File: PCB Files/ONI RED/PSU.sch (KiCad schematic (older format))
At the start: 10 parts

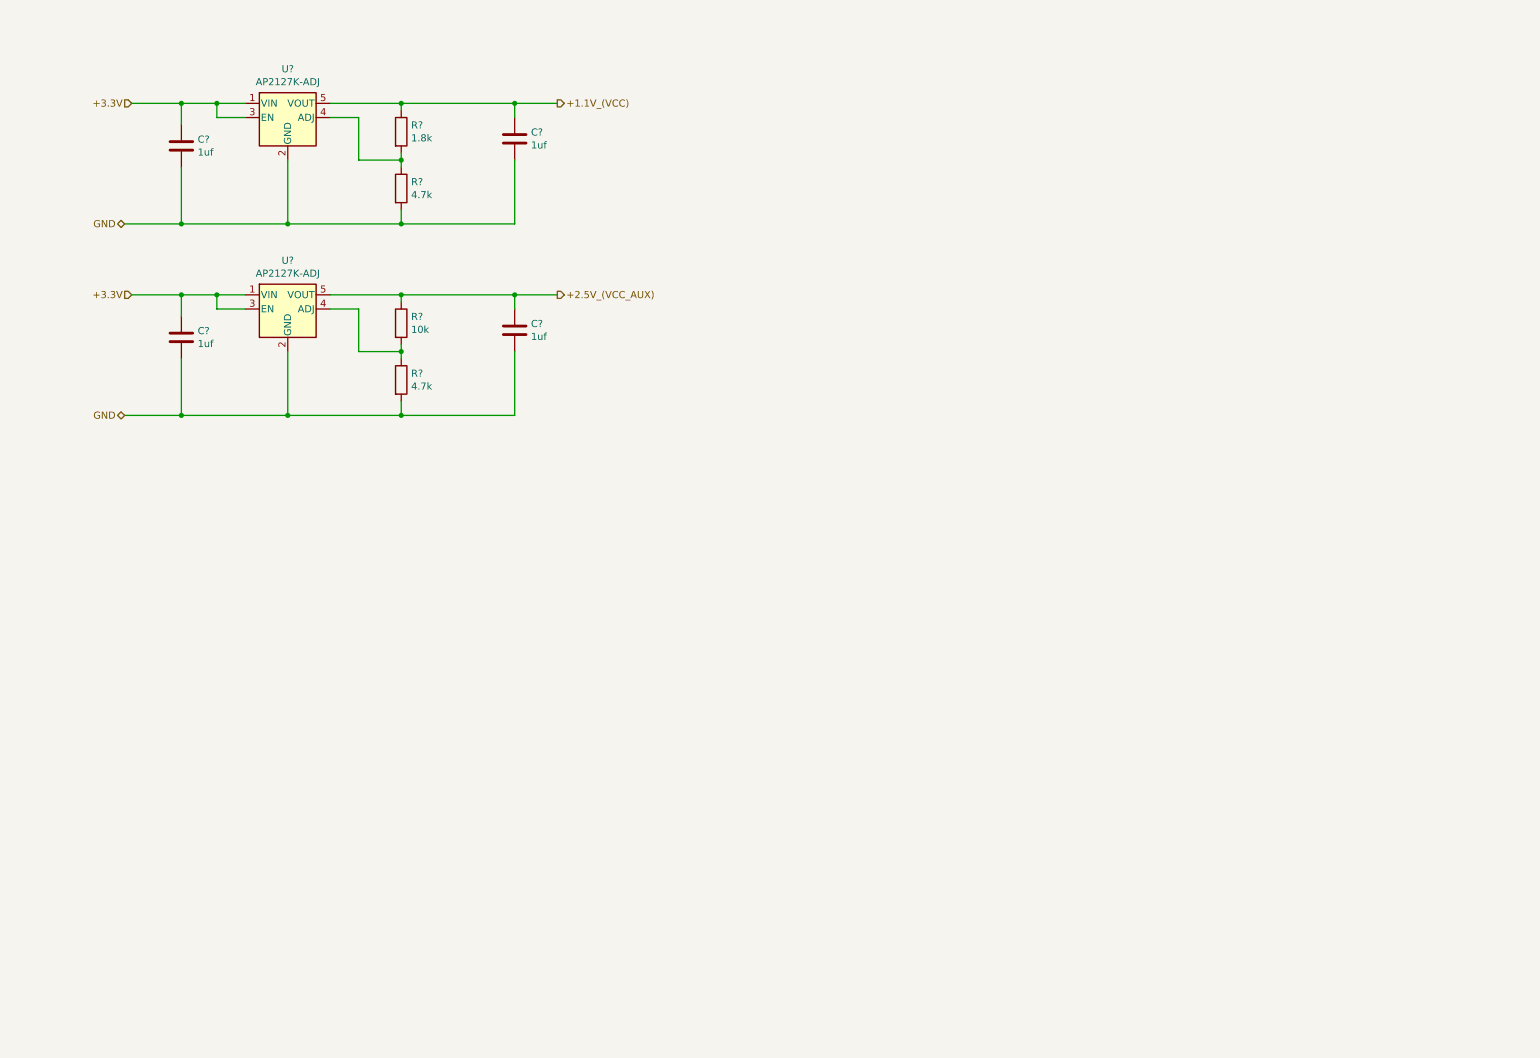
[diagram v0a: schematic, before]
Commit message: Added second ethernet PHY and started to add PCIE connections
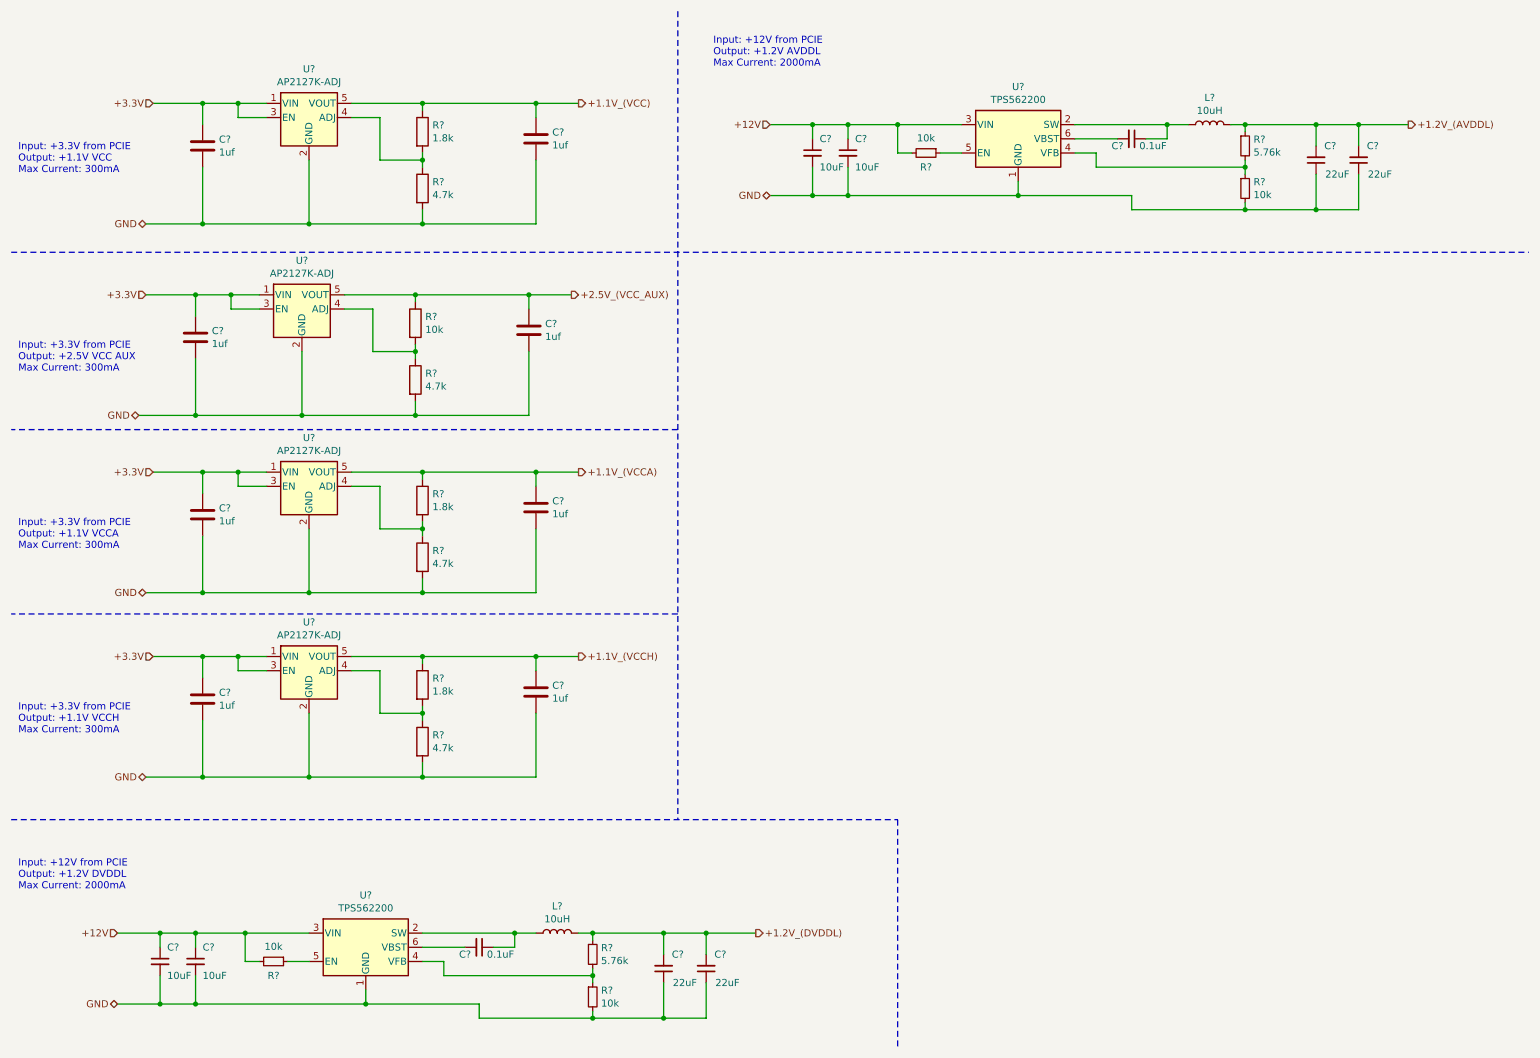
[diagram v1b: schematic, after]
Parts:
- added C? (x4): 1uf, symbol Device:C
- added C? (x4): 10uF, symbol Device:C_Small
- added C? (x2): 0.1uF, symbol Device:C_Small
- added C? (x4): 22uF, symbol Device:C_Small
- added L? (x2): 10uH, symbol Device:L
- added R? (x2): 4.7k, symbol Device:R
- added R? (x2): 1.8k, symbol Device:R
- added R? (x4): 10k, symbol Device:R_Small
- added R? (x2): 5.76k, symbol Device:R_Small
- added U? (x2): AP2127K-ADJ, Package_TO_SOT_SMD:SOT-23-5, symbol Regulator_Linear:AP2127K-ADJ
- added U? (x2): TPS562200, Package_TO_SOT_SMD:SOT-23-6, symbol Regulator_Switching:TPS562200
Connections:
- net +3.3V: now also C?.1, C?.1, U?.1 (VIN), U?.1 (VIN), U?.3 (EN), U?.3 (EN)
- net GND: now also C?.1, C?.1, C?.1, C?.1, C?.2, C?.2, C?.2, C?.2, C?.2, C?.2, C?.2, C?.2, R?.2, R?.2, R?.2, R?.2, U?.1 (GND), U?.1 (GND), U?.2 (GND), U?.2 (GND)
- new net: R?.1, R?.2, U?.4 (ADJ) (x2)
- new net: C?.1, L?.1, U?.2 (SW) (x2)
- new net: R?.1, R?.2, U?.4 (VFB) (x2)
- new net: R?.1, U?.5 (EN) (x2)
- new net: C?.2, U?.6 (VBST) (x2)
- new net +1.1V_(VCCA): C?.1, R?.1, U?.5 (VOUT)
- new net +1.1V_(VCCH): C?.1, R?.1, U?.5 (VOUT)
- new net +1.2V_(AVDDL): C?.2, C?.2, L?.2, R?.1
- new net +1.2V_(DVDDL): C?.2, C?.2, L?.2, R?.1
- new net +12V: C?.1, C?.1, C?.1, C?.1, R?.2, R?.2, U?.3 (VIN), U?.3 (VIN)
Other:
- note added: "Input: +12V from PCIE\nOutput: +1.2V AVDDL\nMax Current: 2000mA"
- note added: "Input: +12V from PCIE\nOutput: +1.2V DVDDL\nMax Current: 2000mA"
- note added: "Input: +3.3V from PCIE\nOutput: +1.1V VCCA\nMax Current: 300mA"
- note added: "Input: +3.3V from PCIE\nOutput: +1.1V VCCH\nMax Current: 300mA"
- note added: "Input: +3.3V from PCIE\nOutput: +1.1V VCC\nMax Current: 300mA"
- note added: "Input: +3.3V from PCIE\nOutput: +2.5V VCC AUX\nMax Current: 300mA\n"
- moved on the sheet: C?, R?, U?

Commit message: Continued routing work
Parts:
- removed C? (x2): 1uf, symbol Device:C
- removed C? (x2): 10uF, symbol Device:C_Small
- removed C?: 0.1uF, symbol Device:C_Small
- removed C? (x2): 22uF, symbol Device:C_Small
- removed L?: 10uH, symbol Device:L
- removed R?: 4.7k, symbol Device:R
- removed R?: 1.8k, symbol Device:R
- removed R? (x2): 10k, symbol Device:R_Small
- removed R?: 5.76k, symbol Device:R_Small
- removed U?: AP2127K-ADJ, Package_TO_SOT_SMD:SOT-23-5, symbol Regulator_Linear:AP2127K-ADJ
- removed U?: TPS562200, Package_TO_SOT_SMD:SOT-23-6, symbol Regulator_Switching:TPS562200
- added C40: 22uF, symbol Device:CP1_Small
- added C41: 0.01uF, symbol Device:CP1_Small
- added C42: 0.1uF, symbol Device:CP1_Small
- added FB1: FB, symbol Device:Ferrite_Bead
- gave numbers to parts that had none: 25
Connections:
- net +1.2V_(AVDDL): now also C40.1, C41.1, C42.1, FB1.1
- net +1.2V_(DVDDL): now also FB1.2
- net GND: now also C40.2, C41.2, C42.2
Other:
- note removed: "Input: +12V from PCIE\nOutput: +1.2V AVDDL\nMax Current: 2000mA"
- note removed: "Input: +3.3V from PCIE\nOutput: +1.1V VCCH\nMax Current: 300mA"
- moved on the sheet: C29, C30, C34, C38, C39, L1, R20, R27, R28, U6
